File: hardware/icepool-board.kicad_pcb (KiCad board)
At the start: 4 copper layers, 140 x 96 mm, 117 parts, among them J1 USB_B_Micro, J10 Conn_02x08_Odd_Even, J11 Conn_02x08_Odd_Even, J12 Conn_02x08_Odd_Even, J13 Conn_02x08_Odd_Even, J14 Conn_02x08_Odd_Even, J15 Conn_02x08_Odd_Even, J16 Conn_02x08_Odd_Even, J17 Conn_02x08_Odd_Even, J18 Conn_02x08_Odd_Even, J19 Conn_02x08_Odd_Even, J2 Conn_01x02, J20 Conn_02x08_Odd_Even, J21 Conn_01x04, J3 PCIe_6pin, J4 Conn_02x08_Odd_Even, J5 Conn_02x08_Odd_Even, J6 Conn_02x08_Odd_Even, J7 Conn_02x08_Odd_Even, J8 Conn_02x08_Odd_Even, J9 Conn_02x08_Odd_Even, U1 FT232H, U2 AP7361C_SOT-89-5, U3 TPS62133, U6 AP7361C_SOT-89-5, U7 AP7361C_SOT-89-5, U8 iCE40HX8K-BG121(121-Ball_caBG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, X1 ASEM1-12.000MHZ, X2 ASEM1-12.000MHZ

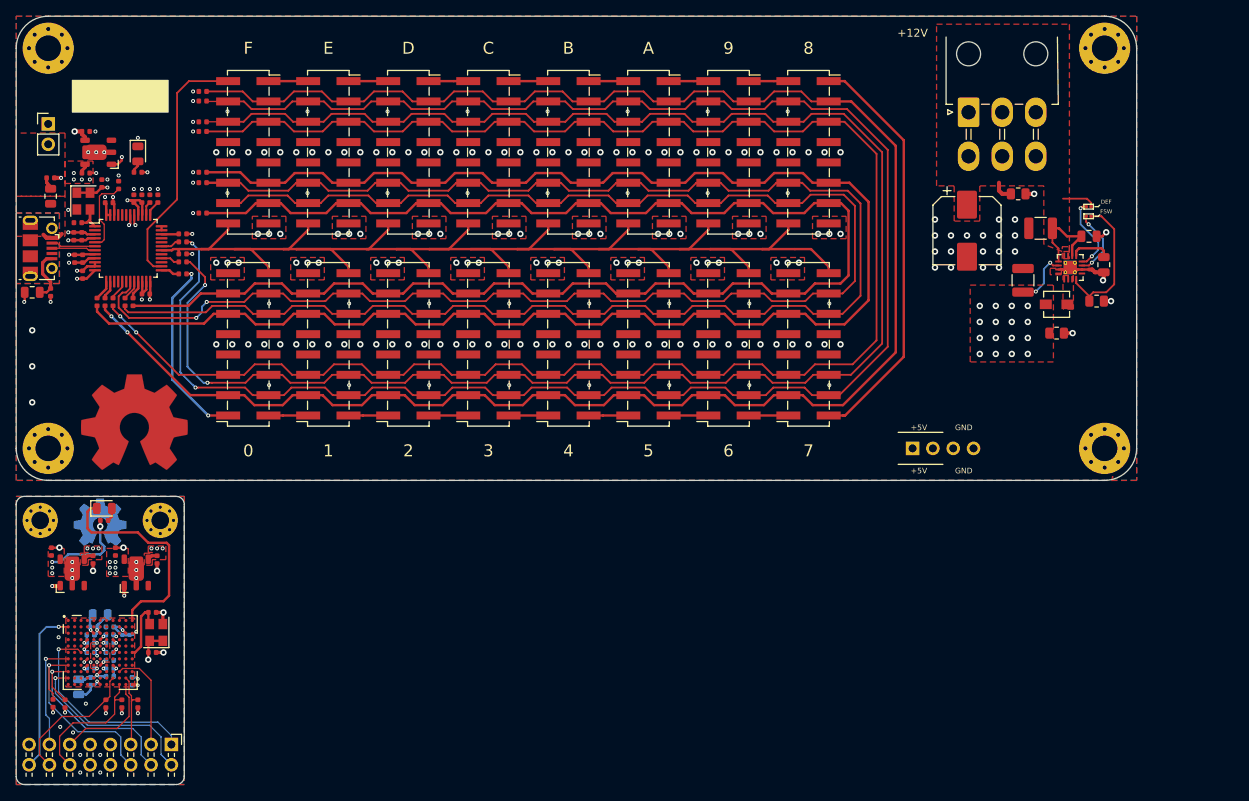
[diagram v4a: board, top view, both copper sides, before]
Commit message: Replaced FT232H with FT2232H for additional SPI interface (issue #45).
Moved +1V2 traces on daughterboard from In1 to In2 (issue #43).

Fixed routing GND, SHIELD on USB (issue #40).
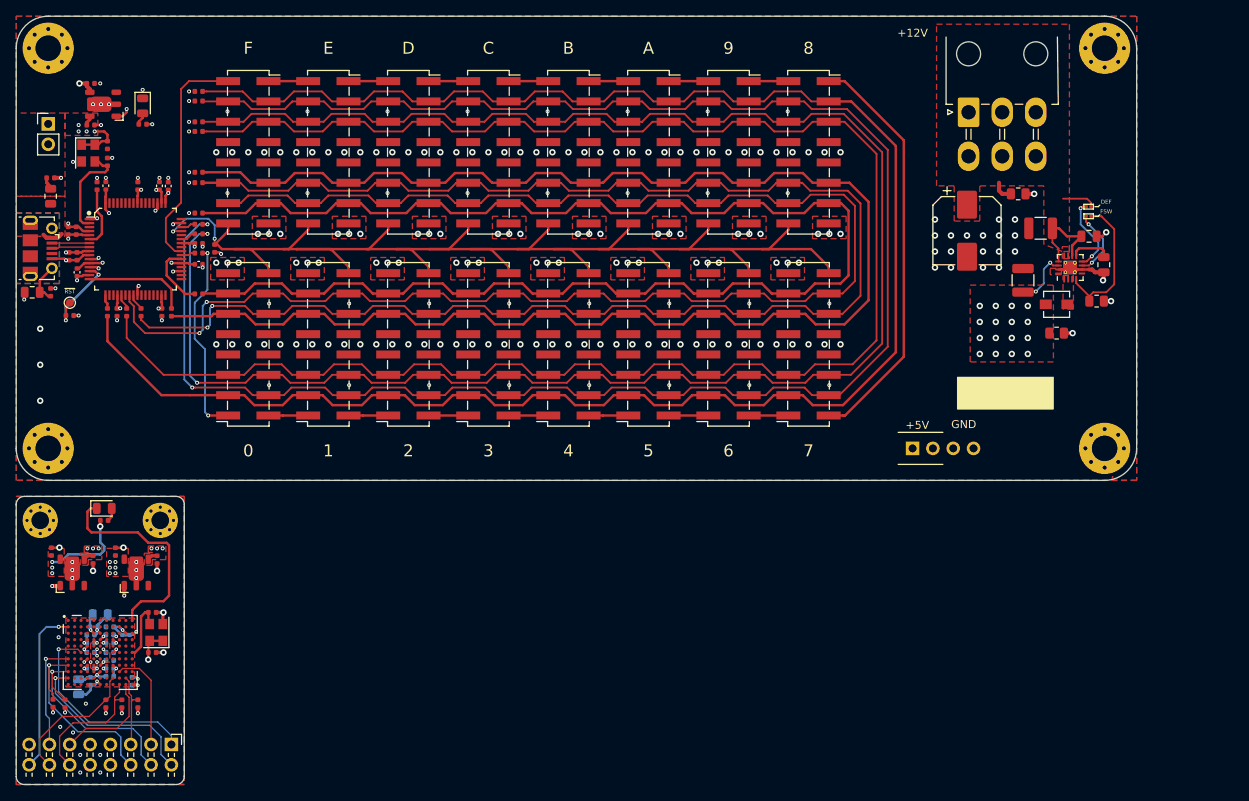
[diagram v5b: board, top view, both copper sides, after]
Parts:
- removed REF**: OSHW-Symbol_6.7x6mm_Copper, Symbol:OSHW-Symbol_6.7x6mm_Copper
- removed REF**: OSHW-Symbol_13.4x12mm_Copper, Symbol:OSHW-Symbol_13.4x12mm_Copper
- added C40: 0.1u, Capacitor_SMD:C_0402_1005Metric, F.Cu at (42.2, 43.2)
- added C43: 4.7u, Capacitor_SMD:C_0402_1005Metric, F.Cu at (50.0, 43.2)
- added TP1: RESET, TestPoint:TestPoint_Pad_D1.0mm, F.Cu at (37.7, 57.8)
- C7: value 0.1u -> 4.7u
- H1, H2, H3, H4: value MountingHole_Pad -> M3_PHT
- J2: value Conn_01x02 -> USE_VBUS_5V
- J21: value Conn_01x04 -> POWER_ALT
- U1: value FT232H -> FT2232HL-REEL; footprint Package_QFP:LQFP-48_7x7mm_P0.5mm -> digikey-footprints:LQFP-64_10x10mm
- moved R6 17.4 mm to (37.7, 59.4)
- moved C5 12.9 mm to (38.6, 54.0), turned to 270 degrees
- moved C50 12.3 mm to (53.8, 50.4), turned to 0 degrees
- moved C6 9.66 mm to (53.8, 53.0), turned to 0 degrees
- moved R2 9.39 mm to (50.4, 59.0)
- moved C10 8.45 mm to (42.4, 40.2), turned to 270 degrees
- moved R7 8.26 mm to (53.8, 56.7), turned to 180 degrees
- moved C18 6.37 mm to (43.6, 59.0), turned to 270 degrees
- moved C11 6.03 mm to (40.3, 30.4)
- moved C12 6.03 mm to (40.3, 35.6)
- moved D1 6.03 mm to (46.8, 33.2)
- moved R1 6.03 mm to (46.8, 35.5)
- moved U2 6.03 mm to (41.9, 33.0)
- moved X1 6.03 mm to (40.0, 39.1)
- moved C8 4.85 mm to (42.4, 38.1), turned to 90 degrees
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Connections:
- C5 pad 1: Net-(C5-Pad1) -> +1V8
- C6 pad 1: Net-(C6-Pad1) -> +1V8
- H1 pad 1: Net-(H1-Pad1) -> GND
- H2 pad 1: Net-(H2-Pad1) -> GND
- H3 pad 1: Net-(H3-Pad1) -> GND
- H4 pad 1: Net-(H4-Pad1) -> GND
- U1 pad 1: /icepool-motherboard/FT_CLK -> GND
- U1 pad 12: +3V3 -> +1V8
- U1 pad 13: Net-(R2-Pad2) -> GND
- U1 pad 14: Net-(R3-Pad2) -> /icepool-motherboard/FT_RST
- U1 pad 15: Net-(U1-Pad15) -> GND
- U1 pad 16: Net-(U1-Pad16) -> Net-(R2-Pad2)
- U1 pad 17: Net-(R4-Pad2) -> Net-(R3-Pad2)
- U1 pad 19: /icepool-motherboard/CDONE -> Net-(U1-Pad19)
- U1 pad 2: Net-(U1-Pad2) -> /icepool-motherboard/FT_CLK
- U1 pad 20: Net-(R5-Pad2) -> +3V3
- U1 pad 21: Net-(R7-Pad2) -> Net-(R4-Pad2)
- U1 pad 22: GND -> Net-(U1-Pad22)
- U1 pad 23: GND -> /icepool-motherboard/CDONE
- U1 pad 24: +3V3 -> Net-(R5-Pad2)
- U1 pad 25: Net-(R8-Pad2) -> GND
- U1 pad 26: /icepool-motherboard/CIPO1 -> Net-(U1-Pad26)
- U1 pad 28: Net-(R11-Pad2) -> Net-(U1-Pad28)
- U1 pad 3: +3V3 -> Net-(U1-Pad3)
- U1 pad 30: /icepool-motherboard/READY -> Net-(U1-Pad30)
- U1 pad 31: Net-(R13-Pad2) -> +3V3
- U1 pad 34: /icepool-motherboard/FT_RST -> Net-(U1-Pad34)
- U1 pad 36: GND -> Net-(U1-Pad36)
- U1 pad 37: Net-(C6-Pad1) -> +1V8
- U1 pad 38: Net-(C5-Pad1) -> Net-(R7-Pad2)
- U1 pad 39: +3V3 -> Net-(R8-Pad2)
- U1 pad 4: GND -> +3V3
- U1 pad 40: +3V3 -> /icepool-motherboard/CIPO1
- U1 pad 41: GND -> Net-(U1-Pad41)
- U1 pad 42: GND -> +3V3
- U1 pad 43: Net-(U1-Pad43) -> Net-(R11-Pad2)
- U1 pad 45: Net-(U1-Pad45) -> /icepool-motherboard/READY
- U1 pad 46: +3V3 -> Net-(R13-Pad2)
- U1 pad 48: GND -> Net-(U1-Pad48)
- U1 pad 5: Net-(R9-Pad1) -> GND
- U1 pad 6: /icepool-motherboard/USB_D- -> Net-(R9-Pad1)
- U1 pad 7: /icepool-motherboard/USB_D+ -> /icepool-motherboard/USB_D-
- U1 pad 8: +3V3 -> /icepool-motherboard/USB_D+
- U1 pad 9: GND -> +3V3
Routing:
- net +1V8: track 0.00 -> 38.4 mm, vias 0 -> 4
- net Net-(R2-Pad2): track 2.53 -> 13.2 mm
- net /icepool-motherboard/SCK0: track 211.2 -> 200.7 mm
- net /icepool-motherboard/FT_RST: track 2.17 -> 11.1 mm, vias 0 -> 2
- net /icepool-motherboard/SCK1: track 194.7 -> 185.9 mm
- net /icepool-motherboard/FT_CLK: track 4.79 -> 12.4 mm
- net Net-(R7-Pad2): track 2.32 -> 8.21 mm
- net /icepool-motherboard/~CS1: track 227.1 -> 231.4 mm
- net /icepool-motherboard/~RW: track 233.6 -> 236.8 mm
- net /icepool-motherboard/CIPO1: track 31.5 -> 28.6 mm
- net +3V3: track 53.7 -> 55.9 mm
- net Net-(R9-Pad1): track 9.75 -> 7.58 mm
- net Net-(C6-Pad1): track 1.95 -> 0.00 mm
- net Net-(C5-Pad1): track 1.74 -> 0.00 mm
- net Net-(C9-Pad1): track 6.56 -> 5.20 mm
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- added copper zone on F.Cu, net +1V2
- removed copper zone on F.Cu, net (none)
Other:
- board text added: "10=AGND"
- board text added: "12=VCORE"
- board text added: "37=VCORE"
- board text added: "49=VREGOUT"
- board text added: "4=VPHY"
- board text added: "50=VREGIN"
- board text added: "64=VCORE"
- board text added: "9=VPLL"
- board text added: "~RST"
- board text removed: "3=VPHY"
- board text removed: "41=AGND"
- board text removed: "4=AGND"
- board text removed: "8 = VPLL"
- board text removed: "9=AGND"

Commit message: Added optional EEPROM for FT2232H (issue #47).
Removed 2021-01 board layout files.

Shoved motherboard headers for more space.

Made bus lines narrower (12mil > 9mil).
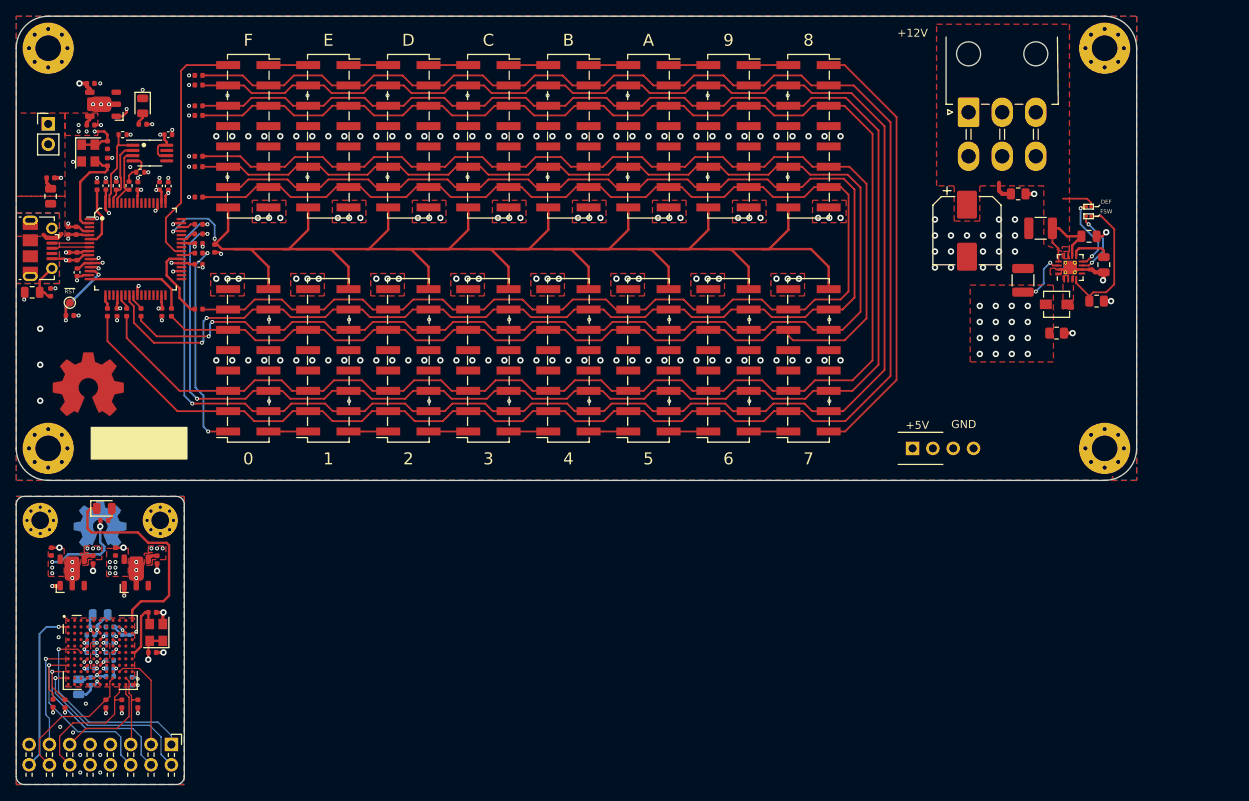
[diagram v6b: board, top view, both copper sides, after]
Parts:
- added C42: 0.1u, Capacitor_SMD:C_0402_1005Metric, F.Cu at (50.0, 36.8)
- added R32: 4k7, Resistor_SMD:R_0402_1005Metric, F.Cu at (44.3, 36.8)
- added R33: 4k7, Resistor_SMD:R_0402_1005Metric, F.Cu at (43.5, 43.2)
- added R34: 4k7, Resistor_SMD:R_0402_1005Metric, F.Cu at (46.5, 41.5)
- added R35: 1k, Resistor_SMD:R_0402_1005Metric, F.Cu at (45.1, 43.2)
- added REF**: OSHW-Symbol_8.9x8mm_Copper, Symbol:OSHW-Symbol_8.9x8mm_Copper, F.Cu at (40.0, 68.0)
- added REF**: OSHW-Symbol_6.7x6mm_Copper, Symbol:OSHW-Symbol_6.7x6mm_Copper, B.Cu at (41.5, 85.5)
- added U4: 93LCxxC, Package_SO:MSOP-8_3x3mm_P0.65mm, F.Cu at (47.7, 39.1)
- R25, R6: value 4.7k -> 4k7
- moved J10 2.00 mm to (90.0, 65.0)
- moved J11 2.00 mm to (110.0, 37.0)
- moved J12 2.00 mm to (100.0, 37.0)
- moved J13 2.00 mm to (100.0, 65.0)
- moved J14 2.00 mm to (110.0, 65.0)
- moved J15 2.00 mm to (90.0, 37.0)
- moved J16 2.00 mm to (80.0, 37.0)
- moved J17 2.00 mm to (120.0, 65.0)
- moved J18 2.00 mm to (130.0, 65.0)
- moved J19 2.00 mm to (70.0, 37.0)
- moved J20 2.00 mm to (60.0, 37.0)
- moved J4 2.00 mm to (60.0, 65.0)
- moved J6 2.00 mm to (70.0, 65.0)
- moved J7 2.00 mm to (130.0, 37.0)
- moved J8 2.00 mm to (120.0, 37.0)
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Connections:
- U1 pad 61: Net-(U1-Pad61) -> /icepool-motherboard/FT_EEDATA
- U1 pad 62: Net-(U1-Pad62) -> /icepool-motherboard/FT_EECLK
- U1 pad 63: Net-(U1-Pad63) -> /icepool-motherboard/FT_EECS
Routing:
- net /icepool-motherboard/READY: track 173.8 -> 205.8 mm
- net /icepool-motherboard/FT_EECS: track 0.00 -> 10.8 mm
- net /icepool-motherboard/FT_EECLK: track 0.00 -> 8.53 mm
- net /icepool-motherboard/FT_EEDATA: track 0.00 -> 8.11 mm
- net +3V3: track 55.9 -> 62.6 mm, vias 31 -> 35
- net /icepool-motherboard/~RW: track 236.8 -> 243.1 mm
- net /icepool-motherboard/~CS1: track 231.4 -> 237.3 mm
- net /icepool-motherboard/SCK0: track 200.7 -> 205.5 mm
- net /icepool-motherboard/COPI0: track 237.4 -> 242.0 mm
- net Net-(R34-Pad2): track 0.00 -> 4.45 mm
- net /icepool-motherboard/~CS0: track 224.4 -> 228.8 mm
- net /icepool-motherboard/SCK1: track 185.9 -> 189.9 mm
- net /icepool-motherboard/CDONE: track 198.5 -> 202.3 mm
- net /icepool-motherboard/CRESET_B: track 201.8 -> 205.5 mm
- net /icepool-motherboard/SDO1_7: track 51.9 -> 55.2 mm
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
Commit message: Added daisy-chained READY for ready-all support.
Reconfigured header pinout on motherboard and ice40hx8k daughter board.

Addresses issue #48.
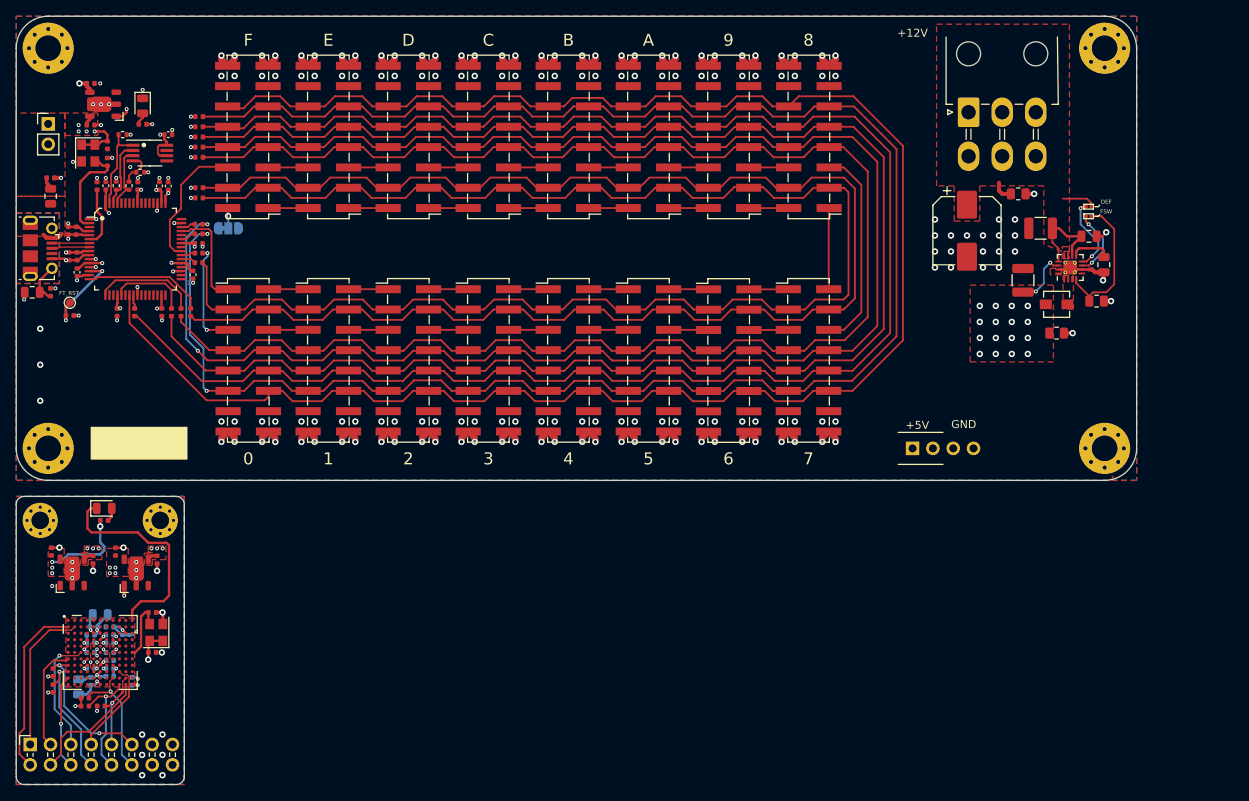
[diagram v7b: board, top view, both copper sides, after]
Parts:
- removed R25: 4k7, Resistor_SMD:R_0402_1005Metric
- removed REF**: OSHW-Symbol_8.9x8mm_Copper, Symbol:OSHW-Symbol_8.9x8mm_Copper
- removed REF**: OSHW-Symbol_6.7x6mm_Copper, Symbol:OSHW-Symbol_6.7x6mm_Copper
- added JP4: Jumper_3_Bridged12, Jumper:SolderJumper-3_P1.3mm_Bridged12_RoundedPad1.0x1.5mm, B.Cu at (57.5, 48.5)
- J10, J11, J12, J13, J14, J15, J16, J17, J18, J19, J4, J6, J7, J8, J9: footprint Connector_PinSocket_2.54mm:PinSocket_2x08_P2.54mm_Vertical_SMD -> Connector_PinHeader_2.54mm:PinHeader_2x08_P2.54mm_Vertical_SMD
- J20: footprint Connector_PinSocket_2.54mm:PinSocket_2x08_P2.54mm_Vertical_SMD -> Connector_PinSocket_2.54mm:PinSocket_2x08_P2.54mm_Horizontal
- J5: footprint Connector_PinHeader_2.54mm:PinHeader_2x08_P2.54mm_Horizontal -> Connector_PinHeader_2.54mm:PinHeader_2x08_P2.54mm_Vertical_SMD
- moved J20 80.7 mm to (32.8, 113.0), turned to 90 degrees
- moved J18 66.2 mm to (70.0, 37.1)
- moved J5 51.9 mm to (70.0, 65.0), turned to 0 degrees
- moved J7 48.8 mm to (90.0, 65.0)
- moved J17 48.8 mm to (80.0, 37.1)
- moved J11 34.4 mm to (130.0, 65.0)
- moved J8 34.4 mm to (100.0, 65.0)
- moved J13 34.3 mm to (120.0, 37.1)
- moved J12 30.0 mm to (130.0, 37.1), turned to 180 degrees
- moved J10 30.0 mm to (120.0, 65.0), turned to 0 degrees
- moved J9 30.0 mm to (110.0, 65.0), turned to 0 degrees
- moved J14 27.9 mm to (110.0, 37.1)
- moved R24 10.2 mm to (53.8, 39.6)
- moved J19 10.1 mm to (59.9, 37.1), turned to 180 degrees
- moved J15 10.0 mm to (100.0, 37.1), turned to 180 degrees
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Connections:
- J10 pad 1: /icepool-motherboard/SDO1_2 -> /icepool-motherboard/~READY_5
- J10 pad 10: GND -> /icepool-motherboard/CRESET_B
- J10 pad 11: /icepool-motherboard/SCK0 -> /icepool-motherboard/~CS1
- J10 pad 12: /icepool-motherboard/CRESET_B -> /icepool-motherboard/CDONE
- J10 pad 13: /icepool-motherboard/SCK1 -> GND
- J10 pad 14: /icepool-motherboard/CDONE -> GND
- J10 pad 16: /icepool-motherboard/READY -> +5V
- J10 pad 2: /icepool-motherboard/SDO1_3 -> /icepool-motherboard/~READY_6
- J10 pad 3: /icepool-motherboard/COPI0 -> /icepool-motherboard/SCK1
- J10 pad 4: /icepool-motherboard/~RW -> /icepool-motherboard/SCK0
- J10 pad 5: /icepool-motherboard/~CS0 -> /icepool-motherboard/SDO1_5
- J10 pad 6: /icepool-motherboard/~CS1 -> /icepool-motherboard/SDO1_6
- J10 pad 7: GND -> /icepool-motherboard/COPI0
- J10 pad 8: GND -> /icepool-motherboard/~RESET
- J10 pad 9: GND -> /icepool-motherboard/~CS0
- J11 pad 1: /icepool-motherboard/SDO1_9 -> /icepool-motherboard/~READY_6
- J11 pad 10: GND -> /icepool-motherboard/CRESET_B
- J11 pad 11: /icepool-motherboard/SCK0 -> /icepool-motherboard/~CS1
- J11 pad 12: /icepool-motherboard/CRESET_B -> /icepool-motherboard/CDONE
- J11 pad 13: /icepool-motherboard/SCK1 -> GND
- J11 pad 14: /icepool-motherboard/CDONE -> GND
- J11 pad 16: /icepool-motherboard/READY -> +5V
- J11 pad 2: /icepool-motherboard/SDO1_10 -> /icepool-motherboard/~READY_7
- J11 pad 3: /icepool-motherboard/COPI0 -> /icepool-motherboard/SCK1
- J11 pad 4: /icepool-motherboard/~RW -> /icepool-motherboard/SCK0
- J11 pad 5: /icepool-motherboard/~CS0 -> /icepool-motherboard/SDO1_6
- J11 pad 6: /icepool-motherboard/~CS1 -> /icepool-motherboard/SDO1_7
- J11 pad 7: GND -> /icepool-motherboard/COPI0
- J11 pad 8: GND -> /icepool-motherboard/~RESET
- J11 pad 9: GND -> /icepool-motherboard/~CS0
- J12 pad 1: /icepool-motherboard/SDO1_10 -> /icepool-motherboard/~READY_7
- J12 pad 10: GND -> /icepool-motherboard/CRESET_B
- J12 pad 11: /icepool-motherboard/SCK0 -> /icepool-motherboard/~CS1
- J12 pad 12: /icepool-motherboard/CRESET_B -> /icepool-motherboard/CDONE
- J12 pad 13: /icepool-motherboard/SCK1 -> GND
- J12 pad 14: /icepool-motherboard/CDONE -> GND
- J12 pad 16: /icepool-motherboard/READY -> +5V
- J12 pad 2: /icepool-motherboard/SDO1_11 -> /icepool-motherboard/~READY_8
- J12 pad 3: /icepool-motherboard/COPI0 -> /icepool-motherboard/SCK1
- J12 pad 4: /icepool-motherboard/~RW -> /icepool-motherboard/SCK0
- J12 pad 5: /icepool-motherboard/~CS0 -> /icepool-motherboard/SDO1_7
- J12 pad 6: /icepool-motherboard/~CS1 -> /icepool-motherboard/SDO1_8
- J12 pad 7: GND -> /icepool-motherboard/COPI0
- J12 pad 8: GND -> /icepool-motherboard/~RESET
- J12 pad 9: GND -> /icepool-motherboard/~CS0
- J13 pad 1: /icepool-motherboard/SDO1_3 -> /icepool-motherboard/~READY_8
- J13 pad 10: GND -> /icepool-motherboard/CRESET_B
- J13 pad 11: /icepool-motherboard/SCK0 -> /icepool-motherboard/~CS1
- J13 pad 12: /icepool-motherboard/CRESET_B -> /icepool-motherboard/CDONE
- J13 pad 13: /icepool-motherboard/SCK1 -> GND
- J13 pad 14: /icepool-motherboard/CDONE -> GND
- J13 pad 16: /icepool-motherboard/READY -> +5V
- J13 pad 2: /icepool-motherboard/SDO1_4 -> /icepool-motherboard/~READY_9
- J13 pad 3: /icepool-motherboard/COPI0 -> /icepool-motherboard/SCK1
- J13 pad 4: /icepool-motherboard/~RW -> /icepool-motherboard/SCK0
- J13 pad 5: /icepool-motherboard/~CS0 -> /icepool-motherboard/SDO1_8
- J13 pad 6: /icepool-motherboard/~CS1 -> /icepool-motherboard/SDO1_9
- J13 pad 7: GND -> /icepool-motherboard/COPI0
- J13 pad 8: GND -> /icepool-motherboard/~RESET
- J13 pad 9: GND -> /icepool-motherboard/~CS0
- J14 pad 1: /icepool-motherboard/SDO1_4 -> /icepool-motherboard/~READY_9
- J14 pad 10: GND -> /icepool-motherboard/CRESET_B
- J14 pad 11: /icepool-motherboard/SCK0 -> /icepool-motherboard/~CS1
- J14 pad 12: /icepool-motherboard/CRESET_B -> /icepool-motherboard/CDONE
- J14 pad 13: /icepool-motherboard/SCK1 -> GND
- J14 pad 14: /icepool-motherboard/CDONE -> GND
- J14 pad 16: /icepool-motherboard/READY -> +5V
- J14 pad 2: /icepool-motherboard/SDO1_5 -> /icepool-motherboard/~READY_10
- J14 pad 3: /icepool-motherboard/COPI0 -> /icepool-motherboard/SCK1
- J14 pad 4: /icepool-motherboard/~RW -> /icepool-motherboard/SCK0
- J14 pad 5: /icepool-motherboard/~CS0 -> /icepool-motherboard/SDO1_9
- J14 pad 6: /icepool-motherboard/~CS1 -> /icepool-motherboard/SDO1_10
- J14 pad 7: GND -> /icepool-motherboard/COPI0
- J14 pad 8: GND -> /icepool-motherboard/~RESET
- J14 pad 9: GND -> /icepool-motherboard/~CS0
- J15 pad 1: /icepool-motherboard/SDO1_11 -> /icepool-motherboard/~READY_10
- J15 pad 10: GND -> /icepool-motherboard/CRESET_B
- J15 pad 11: /icepool-motherboard/SCK0 -> /icepool-motherboard/~CS1
- J15 pad 12: /icepool-motherboard/CRESET_B -> /icepool-motherboard/CDONE
- J15 pad 13: /icepool-motherboard/SCK1 -> GND
- J15 pad 14: /icepool-motherboard/CDONE -> GND
- J15 pad 16: /icepool-motherboard/READY -> +5V
- J15 pad 2: /icepool-motherboard/SDO1_12 -> /icepool-motherboard/~READY_11
- J15 pad 3: /icepool-motherboard/COPI0 -> /icepool-motherboard/SCK1
- J15 pad 4: /icepool-motherboard/~RW -> /icepool-motherboard/SCK0
- J15 pad 5: /icepool-motherboard/~CS0 -> /icepool-motherboard/SDO1_10
- J15 pad 6: /icepool-motherboard/~CS1 -> /icepool-motherboard/SDO1_11
- J15 pad 7: GND -> /icepool-motherboard/COPI0
- J15 pad 8: GND -> /icepool-motherboard/~RESET
- J15 pad 9: GND -> /icepool-motherboard/~CS0
- J16 pad 1: /icepool-motherboard/SDO1_12 -> /icepool-motherboard/~READY_11
- J16 pad 10: GND -> /icepool-motherboard/CRESET_B
- J16 pad 11: /icepool-motherboard/SCK0 -> /icepool-motherboard/~CS1
- J16 pad 12: /icepool-motherboard/CRESET_B -> /icepool-motherboard/CDONE
- J16 pad 13: /icepool-motherboard/SCK1 -> GND
- J16 pad 14: /icepool-motherboard/CDONE -> GND
- J16 pad 16: /icepool-motherboard/READY -> +5V
- J16 pad 2: /icepool-motherboard/SDO1_13 -> /icepool-motherboard/~READY_12
- J16 pad 3: /icepool-motherboard/COPI0 -> /icepool-motherboard/SCK1
- J16 pad 4: /icepool-motherboard/~RW -> /icepool-motherboard/SCK0
- J16 pad 5: /icepool-motherboard/~CS0 -> /icepool-motherboard/SDO1_11
- J16 pad 6: /icepool-motherboard/~CS1 -> /icepool-motherboard/SDO1_12
- J16 pad 7: GND -> /icepool-motherboard/COPI0
- J16 pad 8: GND -> /icepool-motherboard/~RESET
- J16 pad 9: GND -> /icepool-motherboard/~CS0
- J17 pad 1: /icepool-motherboard/SDO1_5 -> /icepool-motherboard/~READY_12
- J17 pad 10: GND -> /icepool-motherboard/CRESET_B
- J17 pad 11: /icepool-motherboard/SCK0 -> /icepool-motherboard/~CS1
- J17 pad 12: /icepool-motherboard/CRESET_B -> /icepool-motherboard/CDONE
- J17 pad 13: /icepool-motherboard/SCK1 -> GND
- J17 pad 14: /icepool-motherboard/CDONE -> GND
- J17 pad 16: /icepool-motherboard/READY -> +5V
- J17 pad 2: /icepool-motherboard/SDO1_6 -> /icepool-motherboard/~READY_13
- J17 pad 3: /icepool-motherboard/COPI0 -> /icepool-motherboard/SCK1
- J17 pad 4: /icepool-motherboard/~RW -> /icepool-motherboard/SCK0
- J17 pad 5: /icepool-motherboard/~CS0 -> /icepool-motherboard/SDO1_12
- J17 pad 6: /icepool-motherboard/~CS1 -> /icepool-motherboard/SDO1_13
- J17 pad 7: GND -> /icepool-motherboard/COPI0
- J17 pad 8: GND -> /icepool-motherboard/~RESET
- J17 pad 9: GND -> /icepool-motherboard/~CS0
- J18 pad 1: /icepool-motherboard/SDO1_6 -> /icepool-motherboard/~READY_13
- J18 pad 10: GND -> /icepool-motherboard/CRESET_B
- J18 pad 11: /icepool-motherboard/SCK0 -> /icepool-motherboard/~CS1
- J18 pad 12: /icepool-motherboard/CRESET_B -> /icepool-motherboard/CDONE
- J18 pad 13: /icepool-motherboard/SCK1 -> GND
- J18 pad 14: /icepool-motherboard/CDONE -> GND
- J18 pad 16: /icepool-motherboard/READY -> +5V
- J18 pad 2: /icepool-motherboard/SDO1_7 -> /icepool-motherboard/~READY_14
- J18 pad 3: /icepool-motherboard/COPI0 -> /icepool-motherboard/SCK1
- J18 pad 4: /icepool-motherboard/~RW -> /icepool-motherboard/SCK0
- J18 pad 5: /icepool-motherboard/~CS0 -> /icepool-motherboard/SDO1_13
- J18 pad 6: /icepool-motherboard/~CS1 -> /icepool-motherboard/SDO1_14
- J18 pad 7: GND -> /icepool-motherboard/COPI0
- J18 pad 8: GND -> /icepool-motherboard/~RESET
- J18 pad 9: GND -> /icepool-motherboard/~CS0
- J19 pad 1: /icepool-motherboard/SDO1_13 -> /icepool-motherboard/~READY_14
- J19 pad 10: GND -> /icepool-motherboard/CRESET_B
- J19 pad 11: /icepool-motherboard/SCK0 -> /icepool-motherboard/~CS1
- J19 pad 12: /icepool-motherboard/CRESET_B -> /icepool-motherboard/CDONE
- J19 pad 13: /icepool-motherboard/SCK1 -> GND
- J19 pad 14: /icepool-motherboard/CDONE -> GND
- J19 pad 16: /icepool-motherboard/READY -> +5V
- J19 pad 2: /icepool-motherboard/SDO1_14 -> /icepool-motherboard/~READY_15
- J19 pad 3: /icepool-motherboard/COPI0 -> /icepool-motherboard/SCK1
- J19 pad 4: /icepool-motherboard/~RW -> /icepool-motherboard/SCK0
- J19 pad 5: /icepool-motherboard/~CS0 -> /icepool-motherboard/SDO1_14
- J19 pad 6: /icepool-motherboard/~CS1 -> /icepool-motherboard/CIPO1
- J19 pad 7: GND -> /icepool-motherboard/COPI0
- J19 pad 8: GND -> /icepool-motherboard/~RESET
- J19 pad 9: GND -> /icepool-motherboard/~CS0
- J20 pad 1: /icepool-motherboard/SDO1_14 -> /ice40hx8k-daughter-board/~READY_OUT
- J20 pad 10: GND -> /ice40hx8k-daughter-board/CRESET_B
- J20 pad 11: /icepool-motherboard/SCK0 -> /ice40hx8k-daughter-board/~CS1
- J20 pad 12: /icepool-motherboard/CRESET_B -> /ice40hx8k-daughter-board/CDONE
- J20 pad 13: /icepool-motherboard/SCK1 -> GND
- J20 pad 14: /icepool-motherboard/CDONE -> GND
- J20 pad 16: /icepool-motherboard/READY -> +5V
- J20 pad 2: /icepool-motherboard/CIPO1 -> /ice40hx8k-daughter-board/~READY_IN
- J20 pad 3: /icepool-motherboard/COPI0 -> /ice40hx8k-daughter-board/SCK1
- J20 pad 4: /icepool-motherboard/~RW -> /ice40hx8k-daughter-board/SCK0
- J20 pad 5: /icepool-motherboard/~CS0 -> /ice40hx8k-daughter-board/SDI1
- J20 pad 6: /icepool-motherboard/~CS1 -> /ice40hx8k-daughter-board/SDO1
- J20 pad 7: GND -> /ice40hx8k-daughter-board/SDI0
- J20 pad 8: GND -> /ice40hx8k-daughter-board/~RESET
- J20 pad 9: GND -> /ice40hx8k-daughter-board/~CS0
- J4 pad 1: /icepool-motherboard/COPI1 -> /icepool-motherboard/~READY
- J4 pad 10: GND -> /icepool-motherboard/CRESET_B
- J4 pad 11: /icepool-motherboard/SCK0 -> /icepool-motherboard/~CS1
- J4 pad 12: /icepool-motherboard/CRESET_B -> /icepool-motherboard/CDONE
- J4 pad 13: /icepool-motherboard/SCK1 -> GND
- J4 pad 14: /icepool-motherboard/CDONE -> GND
- J4 pad 16: /icepool-motherboard/READY -> +5V
- J4 pad 2: /icepool-motherboard/SDO1_0 -> /icepool-motherboard/~READY_0
- J4 pad 3: /icepool-motherboard/COPI0 -> /icepool-motherboard/SCK1
- J4 pad 4: /icepool-motherboard/~RW -> /icepool-motherboard/SCK0
- J4 pad 5: /icepool-motherboard/~CS0 -> /icepool-motherboard/COPI1
- J4 pad 6: /icepool-motherboard/~CS1 -> /icepool-motherboard/SDO1_0
- J4 pad 7: GND -> /icepool-motherboard/COPI0
- J4 pad 8: GND -> /icepool-motherboard/~RESET
- J4 pad 9: GND -> /icepool-motherboard/~CS0
- J5 pad 1: /ice40hx8k-daughter-board/SDI1 -> /icepool-motherboard/~READY_0
- J5 pad 10: GND -> /icepool-motherboard/CRESET_B
- J5 pad 11: /ice40hx8k-daughter-board/SCK0 -> /icepool-motherboard/~CS1
- J5 pad 12: /ice40hx8k-daughter-board/CRESET_B -> /icepool-motherboard/CDONE
- J5 pad 13: /ice40hx8k-daughter-board/SCK1 -> GND
- J5 pad 14: /ice40hx8k-daughter-board/CDONE -> GND
- J5 pad 16: /ice40hx8k-daughter-board/READY -> +5V
- J5 pad 2: /ice40hx8k-daughter-board/SDO1 -> /icepool-motherboard/~READY_1
- J5 pad 3: /ice40hx8k-daughter-board/SDI0 -> /icepool-motherboard/SCK1
- J5 pad 4: /ice40hx8k-daughter-board/~RW -> /icepool-motherboard/SCK0
- J5 pad 5: /ice40hx8k-daughter-board/~CS0 -> /icepool-motherboard/SDO1_0
- J5 pad 6: /ice40hx8k-daughter-board/~CS1 -> /icepool-motherboard/SDO1_1
- J5 pad 7: GND -> /icepool-motherboard/COPI0
- J5 pad 8: GND -> /icepool-motherboard/~RESET
- J5 pad 9: GND -> /icepool-motherboard/~CS0
- J6 pad 1: /icepool-motherboard/SDO1_0 -> /icepool-motherboard/~READY_1
- J6 pad 10: GND -> /icepool-motherboard/CRESET_B
- J6 pad 11: /icepool-motherboard/SCK0 -> /icepool-motherboard/~CS1
- J6 pad 12: /icepool-motherboard/CRESET_B -> /icepool-motherboard/CDONE
- J6 pad 13: /icepool-motherboard/SCK1 -> GND
- J6 pad 14: /icepool-motherboard/CDONE -> GND
- J6 pad 16: /icepool-motherboard/READY -> +5V
- J6 pad 2: /icepool-motherboard/SDO1_1 -> /icepool-motherboard/~READY_2
- J6 pad 3: /icepool-motherboard/COPI0 -> /icepool-motherboard/SCK1
- J6 pad 4: /icepool-motherboard/~RW -> /icepool-motherboard/SCK0
- J6 pad 5: /icepool-motherboard/~CS0 -> /icepool-motherboard/SDO1_1
- J6 pad 6: /icepool-motherboard/~CS1 -> /icepool-motherboard/SDO1_2
- J6 pad 7: GND -> /icepool-motherboard/COPI0
- J6 pad 8: GND -> /icepool-motherboard/~RESET
- J6 pad 9: GND -> /icepool-motherboard/~CS0
- J7 pad 1: /icepool-motherboard/SDO1_7 -> /icepool-motherboard/~READY_2
- J7 pad 10: GND -> /icepool-motherboard/CRESET_B
- J7 pad 11: /icepool-motherboard/SCK0 -> /icepool-motherboard/~CS1
- J7 pad 12: /icepool-motherboard/CRESET_B -> /icepool-motherboard/CDONE
- J7 pad 13: /icepool-motherboard/SCK1 -> GND
- J7 pad 14: /icepool-motherboard/CDONE -> GND
- J7 pad 16: /icepool-motherboard/READY -> +5V
- J7 pad 2: /icepool-motherboard/SDO1_8 -> /icepool-motherboard/~READY_3
- J7 pad 3: /icepool-motherboard/COPI0 -> /icepool-motherboard/SCK1
- J7 pad 4: /icepool-motherboard/~RW -> /icepool-motherboard/SCK0
- J7 pad 5: /icepool-motherboard/~CS0 -> /icepool-motherboard/SDO1_2
- J7 pad 6: /icepool-motherboard/~CS1 -> /icepool-motherboard/SDO1_3
- J7 pad 7: GND -> /icepool-motherboard/COPI0
- J7 pad 8: GND -> /icepool-motherboard/~RESET
- J7 pad 9: GND -> /icepool-motherboard/~CS0
- J8 pad 1: /icepool-motherboard/SDO1_8 -> /icepool-motherboard/~READY_3
- J8 pad 10: GND -> /icepool-motherboard/CRESET_B
- J8 pad 11: /icepool-motherboard/SCK0 -> /icepool-motherboard/~CS1
- J8 pad 12: /icepool-motherboard/CRESET_B -> /icepool-motherboard/CDONE
- J8 pad 13: /icepool-motherboard/SCK1 -> GND
- J8 pad 14: /icepool-motherboard/CDONE -> GND
- J8 pad 16: /icepool-motherboard/READY -> +5V
- J8 pad 2: /icepool-motherboard/SDO1_9 -> /icepool-motherboard/~READY_4
- J8 pad 3: /icepool-motherboard/COPI0 -> /icepool-motherboard/SCK1
- J8 pad 4: /icepool-motherboard/~RW -> /icepool-motherboard/SCK0
- J8 pad 5: /icepool-motherboard/~CS0 -> /icepool-motherboard/SDO1_3
- J8 pad 6: /icepool-motherboard/~CS1 -> /icepool-motherboard/SDO1_4
- J8 pad 7: GND -> /icepool-motherboard/COPI0
- J8 pad 8: GND -> /icepool-motherboard/~RESET
- J8 pad 9: GND -> /icepool-motherboard/~CS0
- J9 pad 1: /icepool-motherboard/SDO1_1 -> /icepool-motherboard/~READY_4
- J9 pad 10: GND -> /icepool-motherboard/CRESET_B
- J9 pad 11: /icepool-motherboard/SCK0 -> /icepool-motherboard/~CS1
- J9 pad 12: /icepool-motherboard/CRESET_B -> /icepool-motherboard/CDONE
- J9 pad 13: /icepool-motherboard/SCK1 -> GND
- J9 pad 14: /icepool-motherboard/CDONE -> GND
- J9 pad 16: /icepool-motherboard/READY -> +5V
- J9 pad 2: /icepool-motherboard/SDO1_2 -> /icepool-motherboard/~READY_5
- J9 pad 3: /icepool-motherboard/COPI0 -> /icepool-motherboard/SCK1
- J9 pad 4: /icepool-motherboard/~RW -> /icepool-motherboard/SCK0
- J9 pad 5: /icepool-motherboard/~CS0 -> /icepool-motherboard/SDO1_4
- J9 pad 6: /icepool-motherboard/~CS1 -> /icepool-motherboard/SDO1_5
- J9 pad 7: GND -> /icepool-motherboard/COPI0
- J9 pad 8: GND -> /icepool-motherboard/~RESET
- J9 pad 9: GND -> /icepool-motherboard/~CS0
- R13 pad 1: /icepool-motherboard/~RW -> /icepool-motherboard/~RESET
- R19 pad 2: /ice40hx8k-daughter-board/~RW -> /ice40hx8k-daughter-board/~RESET
- R29 pad 2: /icepool-motherboard/~RW -> /icepool-motherboard/~RESET
- U1 pad 45: /icepool-motherboard/READY -> /icepool-motherboard/~READY
- U8 pad B1: /ice40hx8k-daughter-board/READY -> /ice40hx8k-daughter-board/~READY_IN
- U8 pad B2: Net-(U8-PadB2) -> /ice40hx8k-daughter-board/~READY_OUT
- U8 pad J1: /ice40hx8k-daughter-board/~RW -> /ice40hx8k-daughter-board/~RESET
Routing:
- net /icepool-motherboard/~RW: track 243.1 -> 0.00 mm, vias 2 -> 0
- net /icepool-motherboard/~RESET: track 0.00 -> 227.0 mm, vias 0 -> 2
- net /icepool-motherboard/READY: track 205.8 -> 0.00 mm, vias 2 -> 0
- net +5V: track 14.1 -> 163.3 mm, vias 76 -> 92
- net /icepool-motherboard/COPI0: track 242.0 -> 207.6 mm
- net /icepool-motherboard/CDONE: track 202.3 -> 234.4 mm, vias 2 -> 0
- net /icepool-motherboard/SDO1_7: track 55.2 -> 25.9 mm
- net /ice40hx8k-daughter-board/~RW: track 26.4 -> 0.00 mm, vias 1 -> 0
- net /ice40hx8k-daughter-board/~READY_IN: track 0.00 -> 22.1 mm
- net /ice40hx8k-daughter-board/READY: track 20.8 -> 0.00 mm, vias 1 -> 0
- net /icepool-motherboard/CRESET_B: track 205.5 -> 226.0 mm, vias 2 -> 0
- net /ice40hx8k-daughter-board/~READY_OUT: track 0.00 -> 18.6 mm
- net /ice40hx8k-daughter-board/~RESET: track 0.00 -> 16.4 mm, vias 0 -> 1
- net /icepool-motherboard/CIPO1: track 30.8 -> 16.8 mm
- net /icepool-motherboard/COPI1: track 26.7 -> 13.3 mm
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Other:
- rule via_min_size: 0.4572 -> 0.45
- board text added: "FT_RST"
- board text removed: "~RST"
